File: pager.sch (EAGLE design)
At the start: 40 parts, among them Q1 25 MHz, Q2 SI2333DS, X1 52745-3090

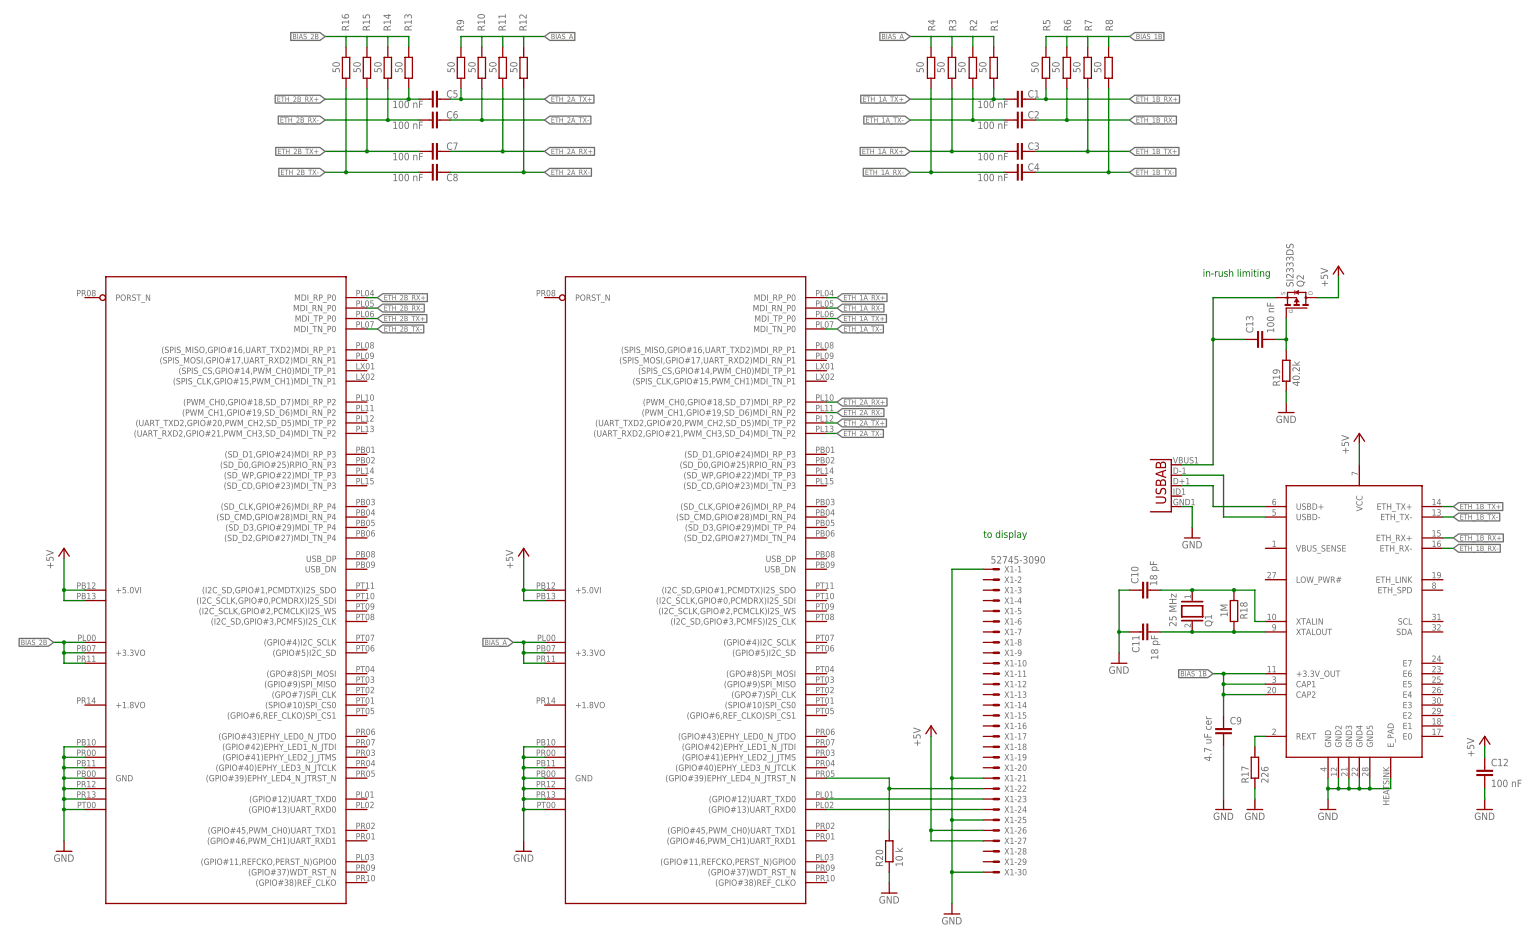
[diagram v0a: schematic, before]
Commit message: Use 0402/0603 capacitors/resistors
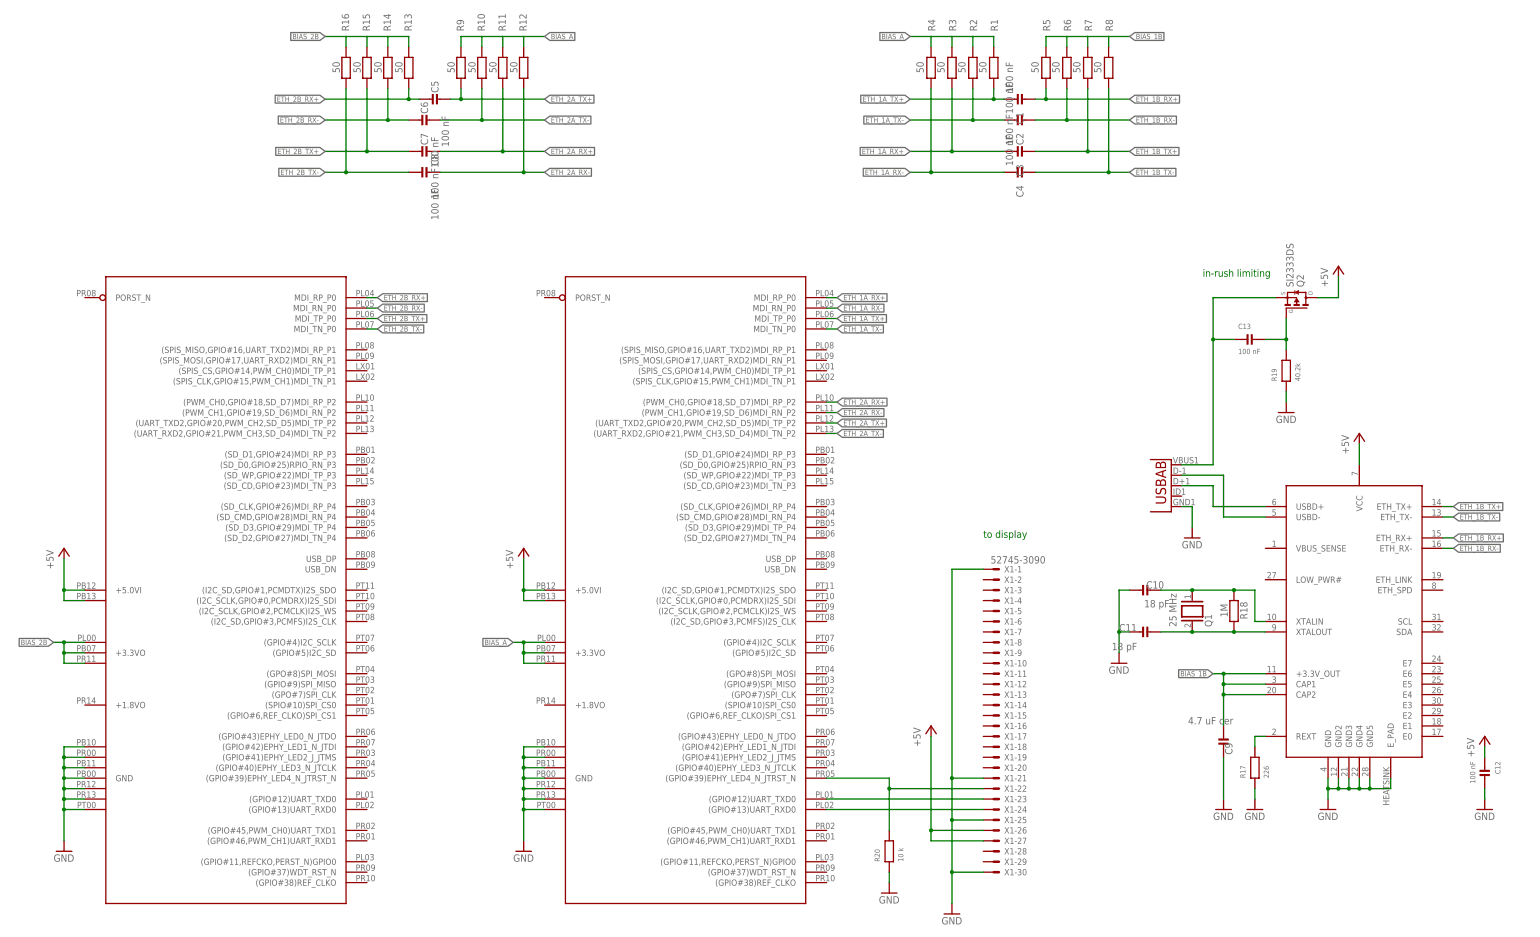
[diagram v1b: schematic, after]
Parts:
- C1, C10, C11, C12, C13, C2, C3, C4, C5, C6, C7, C8: device eagle-ltspice:C -> rc-sysmocom:CAP_CERAMIC_0402
- C9: device eagle-ltspice:C -> rc-sysmocom:CAP_CERAMIC_0603
- R1, R10, R11, R12, R13, R14, R15, R16, R17, R18, R19, R2, R20, R3, R4, R5, R6, R7, R8, R9: device eagle-ltspice:R -> rc-sysmocom:RESISTOR_0402
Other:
- moved on the sheet: C1, C10, C11, C12, C13, C2, C3, C4, C5, C6, C7, C8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

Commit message: Add UART test pads; shrink XTAL package
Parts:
- added TP1, TP2, TP3, TP4: TPTP15R, testpad:TPTP15R
- Q1: device special:XTAL -> laforge:XTAL-ABM3
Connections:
- new net N$29: TP1.TP, U$1.(GPIO#12)UART_TXD0
- new net N$30: TP2.TP, U$1.(GPIO#13)UART_RXD0
- new net N$31: TP3.TP, U$2.(GPIO#12)UART_TXD0
- new net N$32: TP4.TP, U$2.(GPIO#13)UART_RXD0
- net DISP_RX0: now also U$1.(GPIO#45,PWM_CH0)UART_TXD1; no longer U$1.(GPIO#12)UART_TXD0
- net DISP_TX0: now also U$1.(GPIO#46,PWM_CH1)UART_RXD1; no longer U$1.(GPIO#13)UART_RXD0
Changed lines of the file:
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@@
 <part name="GND5" library="supply1" deviceset="GND" device=""/>
 <part name="GND6" library="supply1" deviceset="GND" device=""/>
-<part name="Q1" library="special" deviceset="XTAL" device="" value="25 MHz"/>
+<part name="Q1" library="laforge" deviceset="XTAL" device="-ABM3" value="25 MHz"/>
 <part name="R18" library="rc-sysmocom" deviceset="RESISTOR" device="_0402" value="1M"/>
 <part name="C10" library="rc-sysmocom" deviceset="CAP_CERAMIC" device="_0402" value="18 pF"/>
@@
 <part name="R20" library="rc-sysmocom" deviceset="RESISTOR" device="_0402" value="10 k"/>
 <part name="GND11" library="supply1" deviceset="GND" device=""/>
+<part name="TP1" library="testpad" deviceset="TP" device="TP15R"/>
+<part name="TP2" library="testpad" deviceset="TP" device="TP15R"/>
+<part name="TP3" library="testpad" deviceset="TP" device="TP15R"/>
+<part name="TP4" library="testpad" deviceset="TP" device="TP15R"/>
 </parts>
 <sheets>
@@
 <instance part="R20" gate="G$1" x="30.48" y="-43.18" rot="R90"/>
 <instance part="GND11" gate="1" x="30.48" y="-53.34"/>
+<instance part="TP1" gate="G$1" x="17.78" y="-27.94"/>
+<instance part="TP2" gate="G$1" x="20.32" y="-27.94"/>
+<instance part="TP3" gate="G$1" x="-88.9" y="-25.4"/>
+<instance part="TP4" gate="G$1" x="-86.36" y="-25.4"/>
 </instances>
 <busses>
@@
 <segment>
 <pinref part="X1" gate="-23" pin="S"/>
-<pinref part="U$1" gate="G$1" pin="(GPIO#12)UART_TXD0"/>
-<wire x1="53.34" y1="-30.48" x2="15.24" y2="-30.48" width="0.1524" layer="91"/>
+<wire x1="53.34" y1="-30.48" x2="25.4" y2="-30.48" width="0.1524" layer="91"/>
+<wire x1="25.4" y1="-30.48" x2="25.4" y2="-38.1" width="0.1524" layer="91"/>
+<pinref part="U$1" gate="G$1" pin="(GPIO#45,PWM_CH0)UART_TXD1"/>
+<wire x1="25.4" y1="-38.1" x2="15.24" y2="-38.1" width="0.1524" layer="91"/>
 </segment>
 </net>
@@
 <segment>
 <pinref part="X1" gate="-24" pin="S"/>
-<pinref part="U$1" gate="G$1" pin="(GPIO#13)UART_RXD0"/>
-<wire x1="53.34" y1="-33.02" x2="15.24" y2="-33.02" width="0.1524" layer="91"/>
+<wire x1="53.34" y1="-33.02" x2="27.94" y2="-33.02" width="0.1524" layer="91"/>
+<wire x1="27.94" y1="-33.02" x2="27.94" y2="-40.64" width="0.1524" layer="91"/>
+<pinref part="U$1" gate="G$1" pin="(GPIO#46,PWM_CH1)UART_RXD1"/>
+<wire x1="27.94" y1="-40.64" x2="15.24" y2="-40.64" width="0.1524" layer="91"/>
 </segment>
 </net>
@@
 <wire x1="114.3" y1="10.16" x2="104.14" y2="10.16" width="0.1524" layer="91"/>
 <pinref part="C11" gate="G$1" pin="2"/>
+<wire x1="104.14" y1="12.7" x2="104.14" y2="10.16" width="0.1524" layer="91"/>
 <wire x1="104.14" y1="10.16" x2="96.52" y2="10.16" width="0.1524" layer="91"/>
+<junction x="114.3" y="10.16"/>
 <junction x="104.14" y="10.16"/>
-<junction x="114.3" y="10.16"/>
 </segment>
 </net>
@@
 </segment>
 </net>
+<net name="N$29" class="0">
+<segment>
+<pinref part="U$1" gate="G$1" pin="(GPIO#12)UART_TXD0"/>
+<pinref part="TP1" gate="G$1" pin="TP"/>
+<wire x1="15.24" y1="-30.48" x2="17.78" y2="-30.48" width="0.1524" layer="91"/>
+</segment>
+</net>
+<net name="N$30" class="0">
+<segment>
+<pinref part="U$1" gate="G$1" pin="(GPIO#13)UART_RXD0"/>
+<wire x1="15.24" y1="-33.02" x2="20.32" y2="-33.02" width="0.1524" layer="91"/>
+<pinref part="TP2" gate="G$1" pin="TP"/>
+<wire x1="20.32" y1="-33.02" x2="20.32" y2="-30.48" width="0.1524" layer="91"/>
+</segment>
+</net>
+<net name="N$31" class="0">
+<segment>
+<pinref part="U$2" gate="G$1" pin="(GPIO#12)UART_TXD0"/>
+<pinref part="TP3" gate="G$1" pin="TP"/>
+<wire x1="-96.52" y1="-30.48" x2="-88.9" y2="-30.48" width="0.1524" layer="91"/>
+<wire x1="-88.9" y1="-30.48" x2="-88.9" y2="-27.94" width="0.1524" layer="91"/>
+</segment>
+</net>
+<net name="N$32" class="0">
+<segment>
+<pinref part="U$2" gate="G$1" pin="(GPIO#13)UART_RXD0"/>
+<pinref part="TP4" gate="G$1" pin="TP"/>
+<wire x1="-96.52" y1="-33.02" x2="-86.36" y2="-33.02" width="0.1524" layer="91"/>
+<wire x1="-86.36" y1="-33.02" x2="-86.36" y2="-27.94" width="0.1524" layer="91"/>
+</segment>
+</net>
